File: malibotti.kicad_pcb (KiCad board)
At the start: 2 copper layers, 100 x 55 mm, 23 parts, among them J1 Servos, J2 Servos & I2C, J3 I2C1, J4 I2C2, J5 I2C1, J6 I2C2, U1 ESP32-C3_SUPERMINI_SMD, U2 AS5600, U3 AS5600

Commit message: Improvements
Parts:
- removed D1: LED, liebler_OPTO:LED_1206_3216Metric_ReverseMount
- removed R1: k1, Resistor_SMD:R_1206_3216Metric_Pad1.30x1.75mm_HandSolder
- added C3: u1, Capacitor_SMD:C_1206_3216Metric_Pad1.33x1.80mm_HandSolder, B.Cu at (113.3, 120.9)
- added D21: RGB3, liebler_OPTO:SK6812MINI-E_REV, B.Cu at (117.7, 123.8)
- added J7: RGB, TestPoint:TestPoint_Pad_1.5x1.5mm, B.Cu at (114.8, 125.8)
- added J8: TX, TestPoint:TestPoint_Pad_1.5x1.5mm, B.Cu at (131.9, 107.2)
- added J9: RX, TestPoint:TestPoint_Pad_1.5x1.5mm, B.Cu at (131.9, 109.7)
- added SW8: BTN, liebler_MECH:SW_Push_1P1T_NO_6x6mm_H6.5mm_Reverse, B.Cu at (127.3, 123.8)
- moved R5 25.5 mm to (126.2, 98.9), turned to 180 degrees
- moved R6 23.4 mm to (126.2, 101.2), turned to 180 degrees
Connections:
- U1 pad 10: unconnected-(U1-GPIO10-Pad10) -> SRV1
- U1 pad 20: SRV1 -> /RX
- U1 pad 21: SRV2 -> /TX
- U1 pad 5: Net-(D1-K) -> SCL1
- U1 pad 6: unconnected-(U1-GPIO6-Pad6) -> SDA1
- U1 pad 7: SCL1 -> SRV2
- U1 pad 8: SDA1 -> RGB_LED
- U1 pad 9: unconnected-(U1-GPIO9-Pad9) -> Net-(U1-GPIO9)
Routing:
- net +5V: track 74.0 -> 114.6 mm, vias 4 -> 5
- net Net-(U1-GPIO9): track 0.00 -> 21.4 mm
- net RGB_LED: track 0.00 -> 18.9 mm
- net +3.3V: track 167.8 -> 149.8 mm, vias 2 -> 0
- net SRV2: track 19.1 -> 36.5 mm
- net SRV1: track 27.0 -> 33.9 mm
- net SDA1: track 35.6 -> 30.7 mm
- net Net-(D1-K): track 3.92 -> 0.00 mm
- net /RX: track 0.00 -> 3.50 mm
- net /TX: track 0.00 -> 3.50 mm
- net GND: track 1.21 -> 4.66 mm, vias 86 -> 72
- net Net-(D1-A): track 3.23 -> 0.00 mm
- net Net-(D21-DOUT): track 0.00 -> 1.29 mm
- net SCL1: track 36.6 -> 35.8 mm
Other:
- outline, holes or cut-outs redrawn

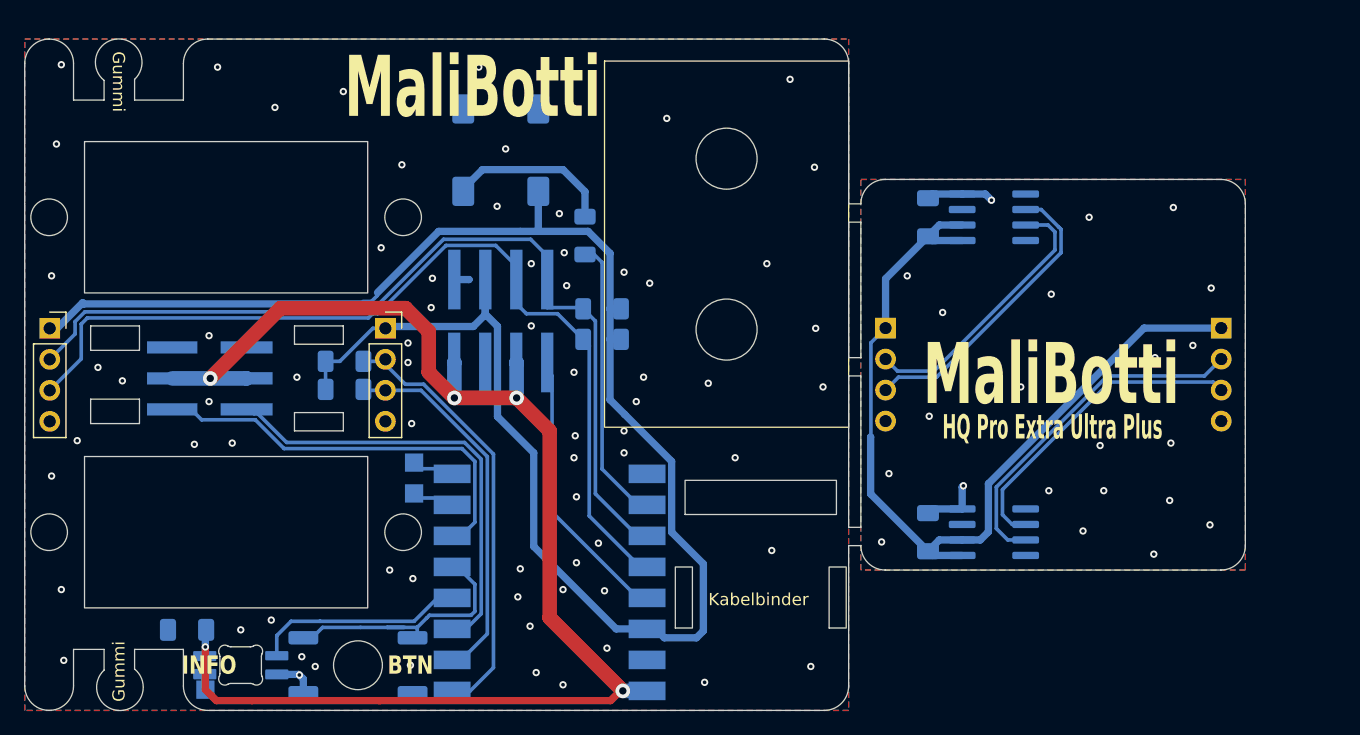
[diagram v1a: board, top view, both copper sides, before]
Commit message: Malibotti as ordered @ JLCPCB
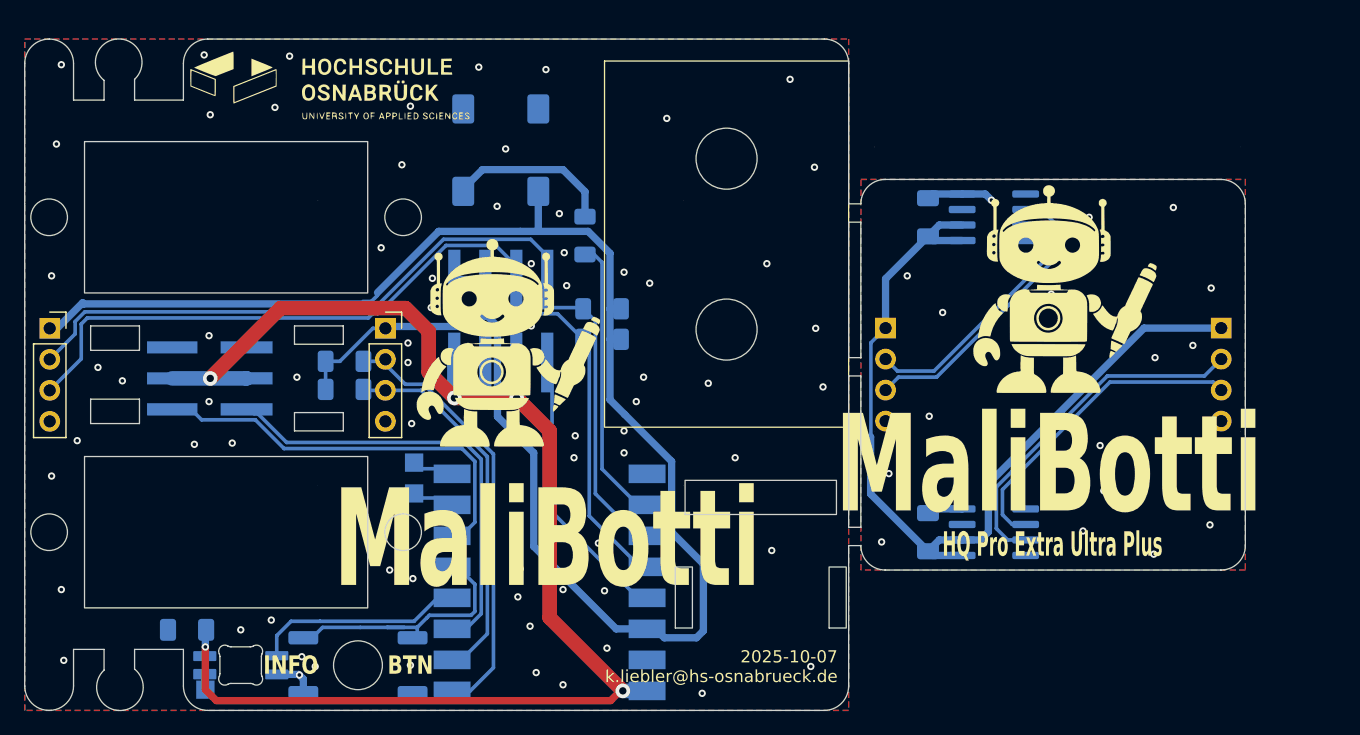
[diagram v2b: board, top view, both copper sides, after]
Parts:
- added G***: LOGO, LOGO, F.Cu at (139.0, 97.4)
- added G***: LOGO, LOGO, F.Cu at (184.6, 93.0)
- added G***: LOGO, LOGO, F.Cu at (125.0, 76.3)
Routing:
- net GND: vias 72 -> 74
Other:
- board text added: "2025-10-07 k.liebler@hs-osnabrueck.de"
- board text removed: "Gummi"
